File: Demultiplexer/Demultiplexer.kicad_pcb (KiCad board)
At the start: 2 copper layers, 3 parts, among them J101 USB_A, U201 74HC74

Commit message: Working on input stage
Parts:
- added C201: 100nF, Capacitor_THT:C_Disc_D5.0mm_W2.5mm_P5.00mm, F.Cu at (88.9, 149.9)
- added C203: 10u, Capacitor_THT:CP_Radial_D4.0mm_P1.50mm, F.Cu at (81.3, 154.9)
- added C204: 10u, Capacitor_THT:CP_Radial_D4.0mm_P1.50mm, F.Cu at (81.3, 165.1)
- added C205: 10u, Capacitor_THT:CP_Radial_D4.0mm_P1.50mm, F.Cu at (102.7, 141.0)
- added D201: LED, LED_THT:LED_D5.0mm, F.Cu at (124.5, 154.9)
- added D202: LED, LED_THT:LED_D5.0mm, F.Cu at (124.5, 165.1)
- added R201: 22k, Resistor_THT:R_Axial_DIN0207_L6.3mm_D2.5mm_P7.62mm_Horizontal, F.Cu at (63.0, 150.1)
- added R202: 22k, Resistor_THT:R_Axial_DIN0207_L6.3mm_D2.5mm_P7.62mm_Horizontal, F.Cu at (52.1, 173.8)
- added R203: 22k, Resistor_THT:R_Axial_DIN0207_L6.3mm_D2.5mm_P7.62mm_Horizontal, F.Cu at (63.0, 146.1)
- added R204: 22k, Resistor_THT:R_Axial_DIN0207_L6.3mm_D2.5mm_P7.62mm_Horizontal, F.Cu at (52.1, 177.8)
- added R205: 4k7, Resistor_THT:R_Axial_DIN0207_L6.3mm_D2.5mm_P7.62mm_Horizontal, F.Cu at (130.8, 154.9)
- added R206: 4k7, Resistor_THT:R_Axial_DIN0207_L6.3mm_D2.5mm_P7.62mm_Horizontal, F.Cu at (130.8, 165.1)
- added R207: 1k, Resistor_THT:R_Axial_DIN0207_L6.3mm_D2.5mm_P7.62mm_Horizontal, F.Cu at (96.5, 130.8)
- added R208: 100k, Resistor_THT:R_Axial_DIN0207_L6.3mm_D2.5mm_P7.62mm_Horizontal, F.Cu at (96.5, 141.0)
- added SW201: SW_Push_Dual, Button_Switch_THT:SW_PUSH_6mm_H4.3mm, F.Cu at (65.3, 155.2)
- added SW202: SW_Push_Dual, Button_Switch_THT:SW_PUSH_6mm_H4.3mm, F.Cu at (65.3, 167.9)
- added U201: 74HC14, Package_DIP:DIP-14_W7.62mm_Socket, F.Cu at (86.4, 154.9)
- moved J101 18.8 mm to (33.6, 170.2)
- renumbered C201 to C202, U201 to U202
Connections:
- U202 pad 1: unconnected-(U201-Pad1) -> /Input Selectors/~{RESET}
- U202 pad 10: unconnected-(U201-Pad10) -> +5V
- U202 pad 11: unconnected-(U201-Pad11) -> Net-(U202-Pad11)
- U202 pad 12: unconnected-(U201-Pad12) -> Net-(U202-Pad12)
- U202 pad 13: unconnected-(U201-Pad13) -> /Input Selectors/~{RESET}
- U202 pad 2: unconnected-(U201-Pad2) -> Net-(U202-Pad2)
- U202 pad 3: unconnected-(U201-Pad3) -> Net-(U202-Pad3)
- U202 pad 4: unconnected-(U201-Pad4) -> +5V
- U202 pad 5: unconnected-(U201-Pad5) -> /Input Selectors/a_{0}
- U202 pad 6: unconnected-(U201-Pad6) -> Net-(U202-Pad2)
- U202 pad 8: unconnected-(U201-Pad8) -> Net-(U202-Pad12)
- U202 pad 9: unconnected-(U201-Pad9) -> /Input Selectors/a_{1}

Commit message: Working on decoder stage
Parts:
- added C301: 100nF, Capacitor_THT:C_Disc_D5.0mm_W2.5mm_P5.00mm, F.Cu at (123.2, 149.9)
- added C401: 100nF, Capacitor_THT:C_Disc_D5.0mm_W2.5mm_P5.00mm, F.Cu at (138.4, 149.9)
- added C402: 100nF, Capacitor_THT:C_Disc_D5.0mm_W2.5mm_P5.00mm, F.Cu at (152.4, 149.9)
- added D301: LED, LED_THT:LED_D3.0mm, F.Cu at (116.8, 104.1)
- added D302: LED, LED_THT:LED_D3.0mm, F.Cu at (94.0, 104.1)
- added D401: LED, LED_THT:LED_D3.0mm, F.Cu at (158.8, 96.5)
- added D402: LED, LED_THT:LED_D3.0mm, F.Cu at (158.8, 83.8)
- added D403: LED, LED_THT:LED_D3.0mm, F.Cu at (158.8, 72.4)
- added D404: LED, LED_THT:LED_D3.0mm, F.Cu at (158.8, 61.0)
- added R301: 4k7, Resistor_THT:R_Axial_DIN0207_L6.3mm_D2.5mm_P7.62mm_Horizontal, F.Cu at (113.0, 111.8)
- added R302: 4k7, Resistor_THT:R_Axial_DIN0207_L6.3mm_D2.5mm_P7.62mm_Horizontal, F.Cu at (90.2, 111.8)
- added R401: 4k7, Resistor_THT:R_Axial_DIN0207_L6.3mm_D2.5mm_P7.62mm_Horizontal, F.Cu at (144.8, 96.5)
- added R402: 4k7, Resistor_THT:R_Axial_DIN0207_L6.3mm_D2.5mm_P7.62mm_Horizontal, F.Cu at (144.8, 83.8)
- added R403: 4k7, Resistor_THT:R_Axial_DIN0207_L6.3mm_D2.5mm_P7.62mm_Horizontal, F.Cu at (144.8, 72.4)
- added R404: 4k7, Resistor_THT:R_Axial_DIN0207_L6.3mm_D2.5mm_P7.62mm_Horizontal, F.Cu at (144.8, 61.0)
- added U301: 74HC00, Package_DIP:DIP-14_W7.62mm_Socket, F.Cu at (121.9, 154.9)
- added U401: 74HC00, Package_DIP:DIP-14_W7.62mm_Socket, F.Cu at (137.2, 154.9)
- added U402: 74HC00, Package_DIP:DIP-14_W7.62mm_Socket, F.Cu at (151.1, 154.9)
- moved R206 61.3 mm to (80.0, 130.8)
- moved D202 56.6 mm to (83.8, 125.7), turned to 90 degrees
- moved C205 45.7 mm to (102.9, 186.7)
- moved R207 45.7 mm to (96.7, 176.5)
- moved R208 45.7 mm to (96.7, 186.7)
- moved SW201 43.9 mm to (104.1, 134.6)
- moved R205 36.4 mm to (103.6, 130.8)
- moved SW202 36.4 mm to (80.6, 134.9)
- moved D201 33.6 mm to (108.0, 125.7), turned to 90 degrees
- moved C201 1.23 mm to (87.7, 149.9)
- moved U202 0.21 mm to (102.9, 154.9)
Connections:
- net /Input Selectors/a_{0} renamed /Decoder/a_{0}
- net /Input Selectors/a_{1} renamed /Decoder/a_{1}

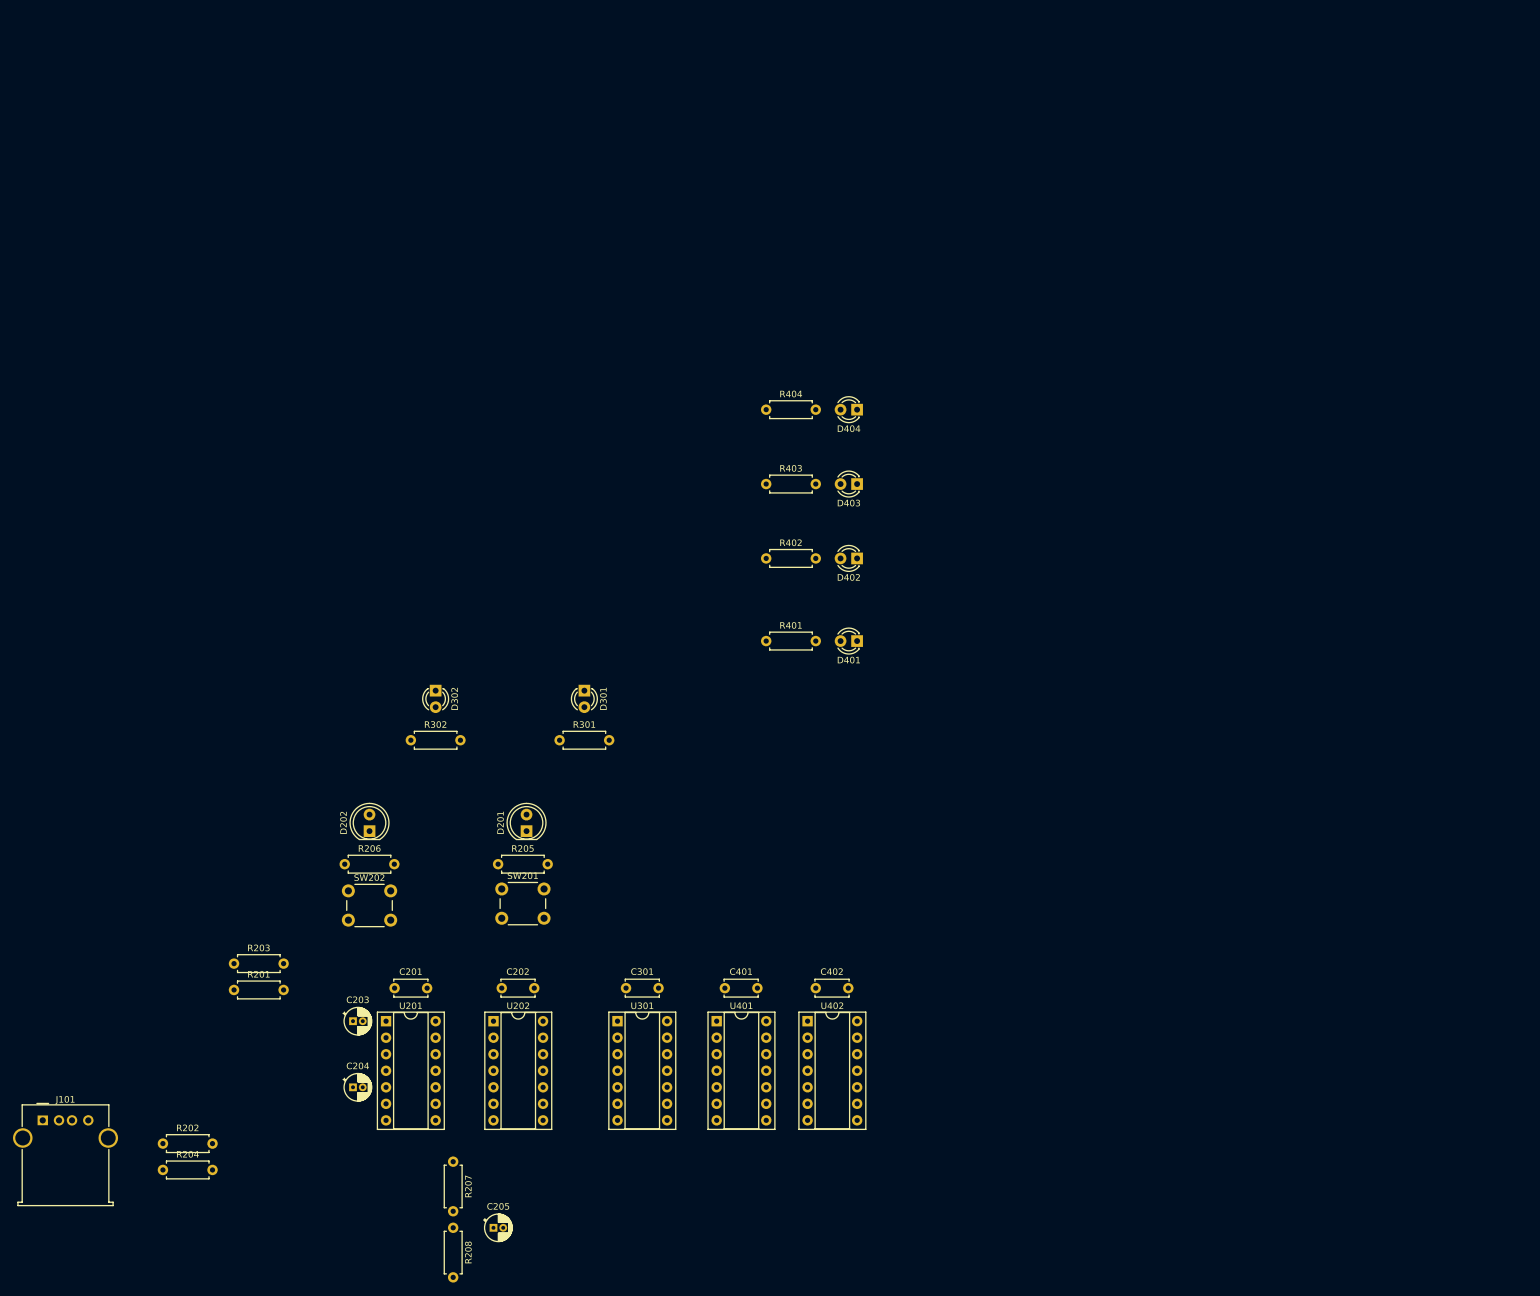
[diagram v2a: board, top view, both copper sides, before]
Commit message: Go with individual chips for AND gates
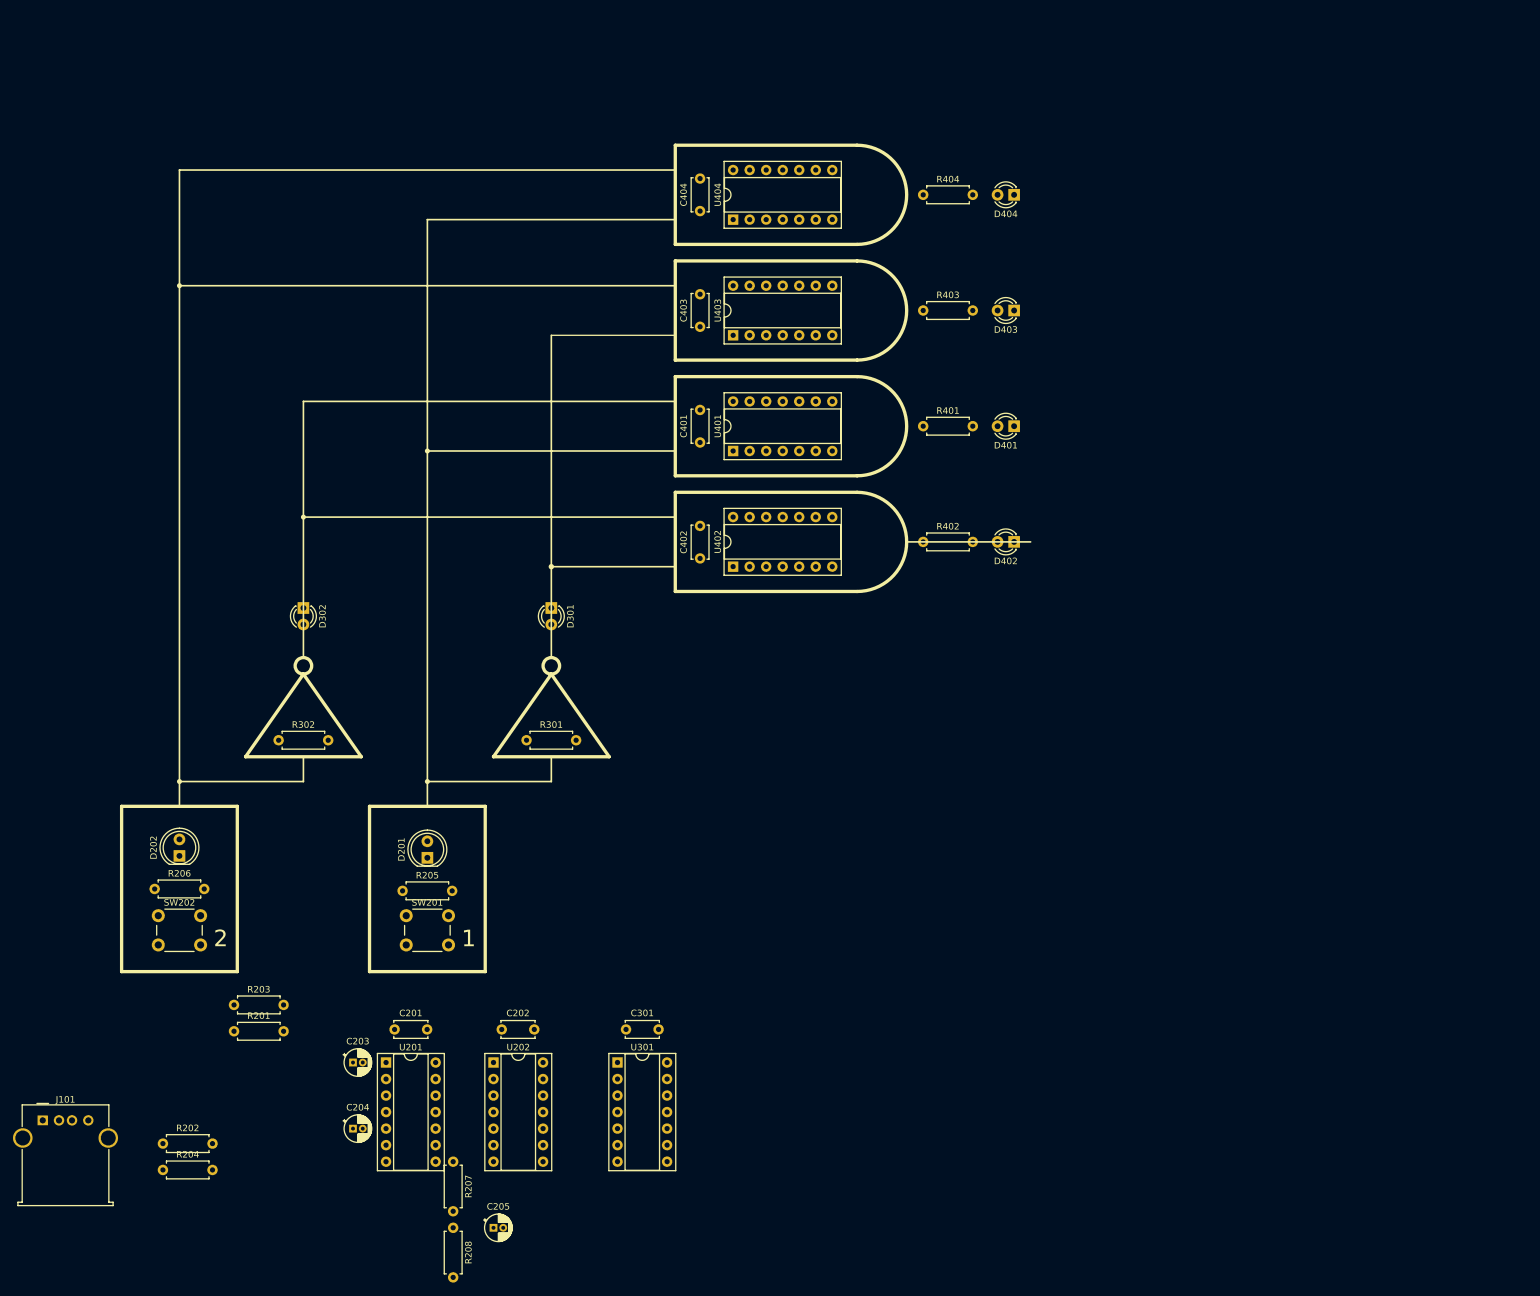
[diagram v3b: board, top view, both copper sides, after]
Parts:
- added C403: 100nF, Capacitor_THT:C_Disc_D5.0mm_W2.5mm_P5.00mm, F.Cu at (134.6, 48.2)
- added C404: 100nF, Capacitor_THT:C_Disc_D5.0mm_W2.5mm_P5.00mm, F.Cu at (134.6, 30.4)
- added U403: 74HC00, Package_DIP:DIP-14_W7.62mm_Socket, F.Cu at (139.7, 49.5)
- added U404: 74HC00, Package_DIP:DIP-14_W7.62mm_Socket, F.Cu at (139.7, 31.8)
- moved U401 87.7 mm to (139.7, 67.3), turned to 90 degrees
- moved C401 83.9 mm to (134.6, 66.0), turned to 90 degrees
- moved U402 70.8 mm to (139.7, 85.1), turned to 90 degrees
- moved C402 68.4 mm to (134.6, 83.8), turned to 90 degrees
- moved D401 40.9 mm to (182.9, 63.5)
- moved D404 40.9 mm to (182.9, 27.9)
- moved R401 40.9 mm to (168.9, 63.5)
- moved R404 40.9 mm to (168.9, 27.9)
- moved D403 36.0 mm to (182.9, 45.7)
- moved R403 36.0 mm to (168.9, 45.7)
- moved R206 29.5 mm to (50.8, 134.6)
- moved D202 29.5 mm to (54.6, 129.5)
- moved SW202 29.5 mm to (51.4, 138.7)
- moved D402 24.3 mm to (182.9, 81.3)
- moved R402 24.3 mm to (168.9, 81.3)
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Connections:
- U401 pad 10: /Decoder/a_{0} -> GND
- U401 pad 11: /Decoder/SELECT1 -> unconnected-(U401-Pad11)
- U401 pad 12: Net-(U401-Pad12) -> GND
- U401 pad 13: Net-(U401-Pad12) -> GND
- U401 pad 8: Net-(U401-Pad12) -> unconnected-(U401-Pad8)
- U401 pad 9: /Decoder/~{a_{1}} -> GND
- U402 pad 1: /Decoder/a_{1} -> /Decoder/~{a_{1}}
- U402 pad 10: /Decoder/a_{0} -> GND
- U402 pad 11: /Decoder/SELECT3 -> unconnected-(U402-Pad11)
- U402 pad 12: Net-(U402-Pad12) -> GND
- U402 pad 13: Net-(U402-Pad12) -> GND
- U402 pad 2: /Decoder/~{a_{0}} -> /Decoder/a_{0}
- U402 pad 6: /Decoder/SELECT2 -> /Decoder/SELECT1
- U402 pad 8: Net-(U402-Pad12) -> unconnected-(U402-Pad8)
- U402 pad 9: /Decoder/a_{1} -> GND
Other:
- board text added: "1"
- board text added: "2"

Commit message: Rethinking NOT gates and starting on output
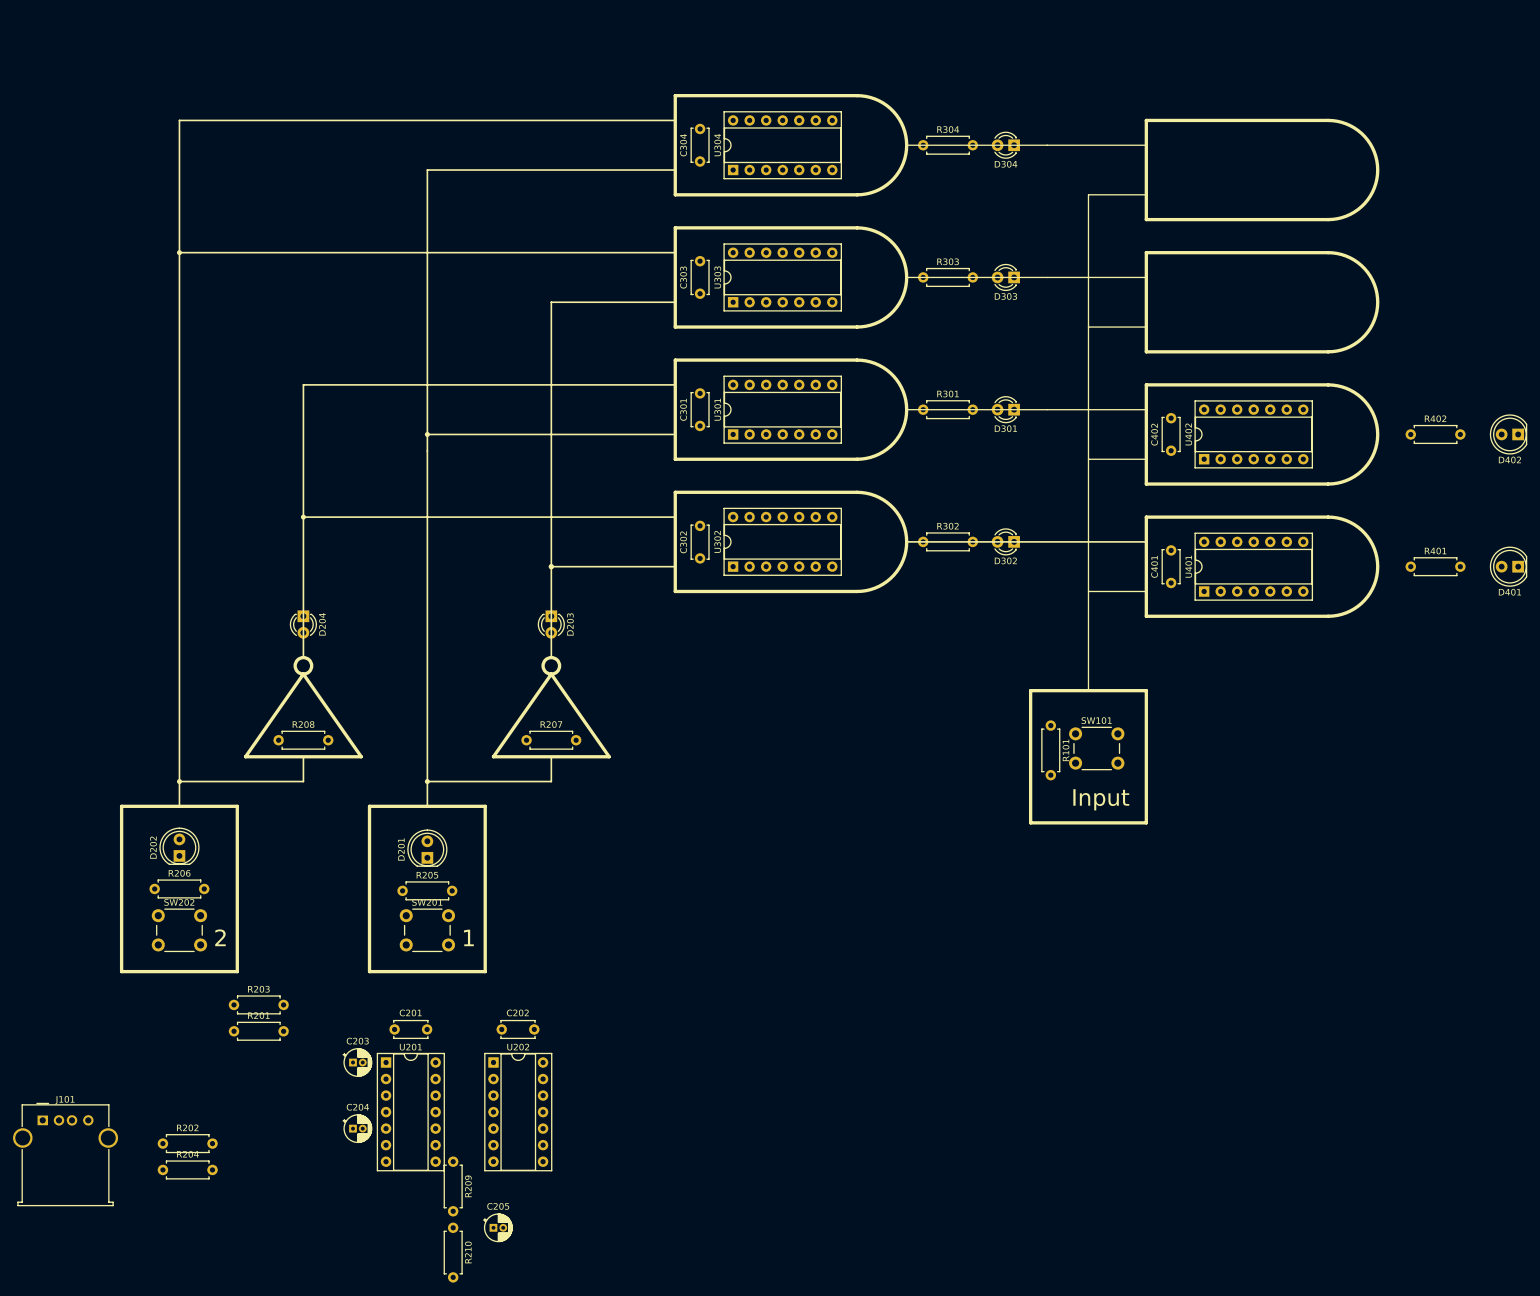
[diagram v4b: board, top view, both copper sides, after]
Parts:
- removed the C301 at (123.2, 156.2)
- removed the D301 at (111.8, 91.4)
- removed the D302 at (73.7, 91.4)
- removed the R301 at (108.0, 111.8)
- removed the R302 at (69.8, 111.8)
- removed the U301 at (121.9, 161.3)
- added C401: 100nF, Capacitor_THT:C_Disc_D5.0mm_W2.5mm_P5.00mm, F.Cu at (207.0, 87.6)
- added C402: 100nF, Capacitor_THT:C_Disc_D5.0mm_W2.5mm_P5.00mm, F.Cu at (207.0, 67.3)
- added D203: LED, LED_THT:LED_D3.0mm, F.Cu at (111.8, 92.7)
- added D204: LED, LED_THT:LED_D3.0mm, F.Cu at (73.7, 92.7)
- added D401: LED, LED_THT:LED_D5.0mm, F.Cu at (260.4, 85.1)
- added D402: LED, LED_THT:LED_D5.0mm, F.Cu at (260.4, 64.8)
- added R101: 100k, Resistor_THT:R_Axial_DIN0207_L6.3mm_D2.5mm_P7.62mm_Horizontal, F.Cu at (188.5, 109.5)
- added R207: 4k7, Resistor_THT:R_Axial_DIN0207_L6.3mm_D2.5mm_P7.62mm_Horizontal, F.Cu at (108.0, 111.8)
- added R208: 4k7, Resistor_THT:R_Axial_DIN0207_L6.3mm_D2.5mm_P7.62mm_Horizontal, F.Cu at (69.8, 111.8)
- added R401: 4k7, Resistor_THT:R_Axial_DIN0207_L6.3mm_D2.5mm_P7.62mm_Horizontal, F.Cu at (243.8, 85.1)
- added R402: 4k7, Resistor_THT:R_Axial_DIN0207_L6.3mm_D2.5mm_P7.62mm_Horizontal, F.Cu at (243.8, 64.8)
- added SW101: SW_Push_Dual, Button_Switch_THT:SW_PUSH_6mm_H4.3mm, F.Cu at (192.3, 110.8)
- added U401: 74HC00, Package_DIP:DIP-14_W7.62mm_Socket, F.Cu at (212.1, 88.9)
- added U402: 74HC00, Package_DIP:DIP-14_W7.62mm_Socket, F.Cu at (212.1, 68.6)
- moved C304 7.62 mm to (134.6, 22.8)
- moved D304 7.62 mm to (182.9, 20.3)
- moved R304 7.62 mm to (168.9, 20.3)
- moved U304 7.62 mm to (139.7, 24.1)
- moved C303 5.08 mm to (134.6, 43.1)
- moved D303 5.08 mm to (182.9, 40.6)
- moved R303 5.08 mm to (168.9, 40.6)
- moved U303 5.08 mm to (139.7, 44.5)
- moved U301 2.54 mm to (139.7, 64.8)
- moved C301 2.54 mm to (134.6, 63.5)
- moved D301 2.54 mm to (182.9, 61.0)
- moved R301 2.54 mm to (168.9, 61.0)
- renumbered C401 to C301, C402 to C302, C403 to C303, C404 to C304, D401 to D301, D402 to D302, D403 to D303, D404 to D304, R207 to R209, R208 to R210, R401 to R301, R402 to R302, R403 to R303, R404 to R304, U401 to U301, U402 to U302, U403 to U303, U404 to U304
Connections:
- U202 pad 12: Net-(U202-Pad12) -> /Decoder/~{a_{1}}
- U202 pad 2: Net-(U202-Pad2) -> /Decoder/~{a_{0}}
- U202 pad 6: Net-(U202-Pad2) -> /Decoder/~{a_{0}}
- U202 pad 8: Net-(U202-Pad12) -> /Decoder/~{a_{1}}
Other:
- board text added: "Input"

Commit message: Finish roughing out board
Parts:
- added C403: 100nF, Capacitor_THT:C_Disc_D5.0mm_W2.5mm_P5.00mm, F.Cu at (198.1, 47.0)
- added C404: 100nF, Capacitor_THT:C_Disc_D5.0mm_W2.5mm_P5.00mm, F.Cu at (198.1, 26.6)
- added D403: LED, LED_THT:LED_D5.0mm, F.Cu at (246.4, 44.5)
- added D404: LED, LED_THT:LED_D5.0mm, F.Cu at (246.4, 24.1)
- added R403: 4k7, Resistor_THT:R_Axial_DIN0207_L6.3mm_D2.5mm_P7.62mm_Horizontal, F.Cu at (232.4, 44.5)
- added R404: 4k7, Resistor_THT:R_Axial_DIN0207_L6.3mm_D2.5mm_P7.62mm_Horizontal, F.Cu at (232.4, 24.1)
- added U403: 74HC00, Package_DIP:DIP-14_W7.62mm_Socket, F.Cu at (203.2, 48.2)
- added U404: 74HC00, Package_DIP:DIP-14_W7.62mm_Socket, F.Cu at (203.9, 27.9)
- moved J101 200.2 mm to (229.9, 130.8)
- moved R209 85.8 mm to (163.8, 123.2)
- moved R210 85.0 mm to (163.8, 134.6)
- moved C205 83.1 mm to (167.6, 134.6)
- moved R204 73.6 mm to (114.3, 138.4)
- moved R202 69.2 mm to (114.3, 143.5)
- moved R203 56.7 mm to (114.3, 128.3)
- moved C202 56.4 mm to (149.9, 123.2)
- moved U201 56.4 mm to (132.1, 128.3)
- moved C201 56.4 mm to (133.4, 123.2)
- moved U202 56.4 mm to (148.6, 128.3)
- moved R201 56.3 mm to (114.3, 133.3)
- moved C203 54.6 mm to (125.7, 129.5)
- moved C204 54.6 mm to (125.7, 139.7)
- moved C302 22.2 mm to (125.7, 63.5)
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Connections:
- R201 pad 1: +5V -> Net-(R203-Pad1)
- R201 pad 2: Net-(R201-Pad2) -> +5V
- R202 pad 1: +5V -> Net-(R204-Pad1)
- R202 pad 2: Net-(R202-Pad2) -> +5V
- R203 pad 1: Net-(R201-Pad2) -> Net-(R203-Pad1)
- R204 pad 1: Net-(R202-Pad2) -> Net-(R204-Pad1)
- SW201 pad 1: Net-(R201-Pad2) -> Net-(R203-Pad1)
- SW202 pad 1: Net-(R202-Pad2) -> Net-(R204-Pad1)
- U402 pad 2: /Output/SELECT1 -> /Decoder/SELECT1
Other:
- board text added: "Ouput 0"
- board text added: "Ouput 1"
- board text added: "Ouput 2"
- board text added: "Ouput 3"
